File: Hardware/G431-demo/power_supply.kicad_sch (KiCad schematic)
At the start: 3 parts, among them U2 NCV8114ASN330T1G

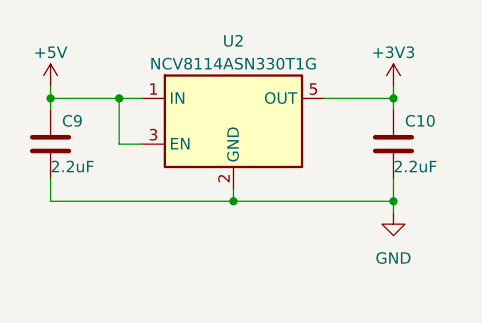
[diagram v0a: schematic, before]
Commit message: Schemetic done; PCB component layout
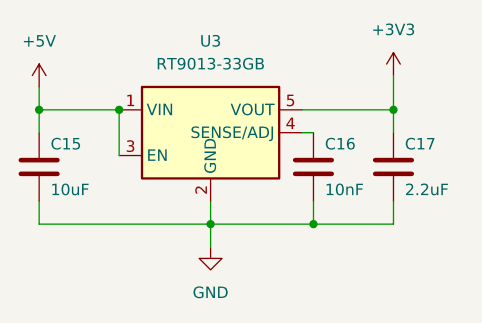
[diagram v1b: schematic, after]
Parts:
- removed C10, C9: 2.2uF, Capacitor_SMD:C_0603_1608Metric, symbol Device:C
- removed U2: NCV8114ASN330T1G, Package_TO_SOT_SMD:TSOT-23-5, symbol Regulator_Linear:NCV8114ASN330T1G
- added C15: 10uF, Capacitor_SMD:C_1206_3216Metric, symbol Device:C
- added C16: 10nF, Capacitor_SMD:C_0603_1608Metric, symbol Device:C
- added C17: 2.2uF, Capacitor_SMD:C_1206_3216Metric, symbol Device:C
- added U3: RT9013-33GB, Package_TO_SOT_SMD:TSOT-23-5, symbol Regulator_Linear:ADP7142AUJZ-3.3
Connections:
- net +3V3: now also C17.1, U3.5 (VOUT)
- net +5V: now also C15.1, U3.1 (VIN), U3.3 (EN)
- net GND: now also C15.2, C16.2, C17.2, U3.2 (GND)
- new net: C16.1, U3.4 (SENSE/ADJ)
